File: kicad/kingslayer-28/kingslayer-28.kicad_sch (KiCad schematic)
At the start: 83 parts, among them IC1 STM32F303CCT7, IC3 LM3940IMP-3.3_NOPB, J1 Conn_01x04_Pin, K1 KEYSW, K10 KEYSW, K11 KEYSW, K12 KEYSW, K13 KEYSW, K14 KEYSW, K15 KEYSW, K16 KEYSW, K17 KEYSW, K18 KEYSW, K19 KEYSW, K2 KEYSW, K20 KEYSW, K21 KEYSW, K22 KEYSW, K23 KEYSW, K24 KEYSW, K25 KEYSW, K26 KEYSW, K27 KEYSW, K28 KEYSW, K3 KEYSW, K4 KEYSW, K5 KEYSW, K6 KEYSW, K7 KEYSW, K8 KEYSW, K9 KEYSW, SW1 SS12D07, X1 IC21008.000M30.0EE1B

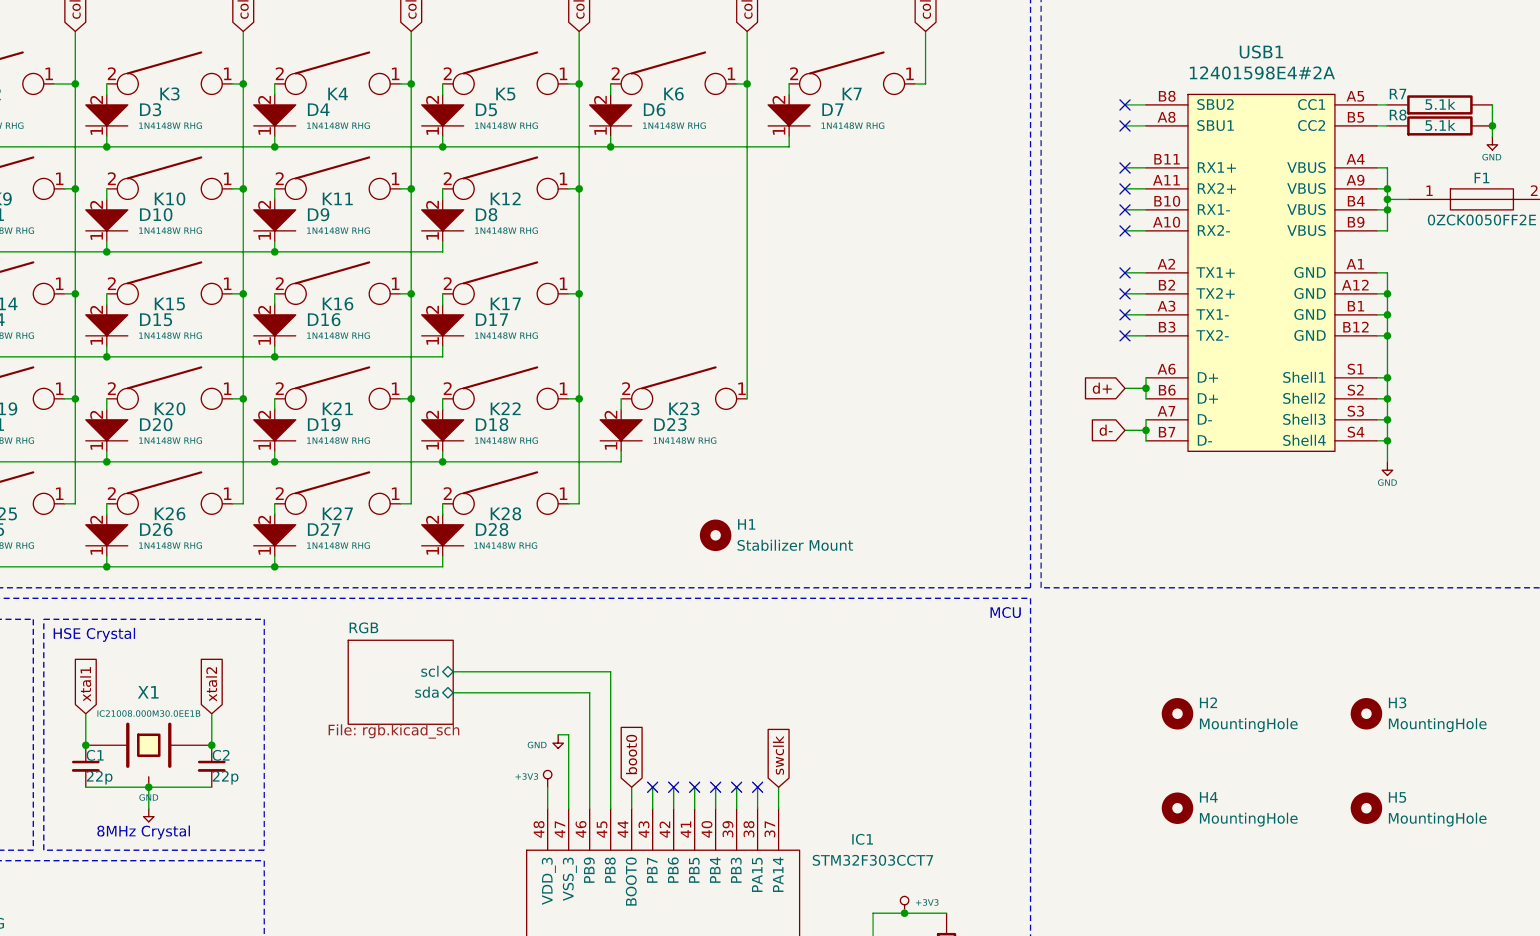
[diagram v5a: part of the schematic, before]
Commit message: finish footprint picking
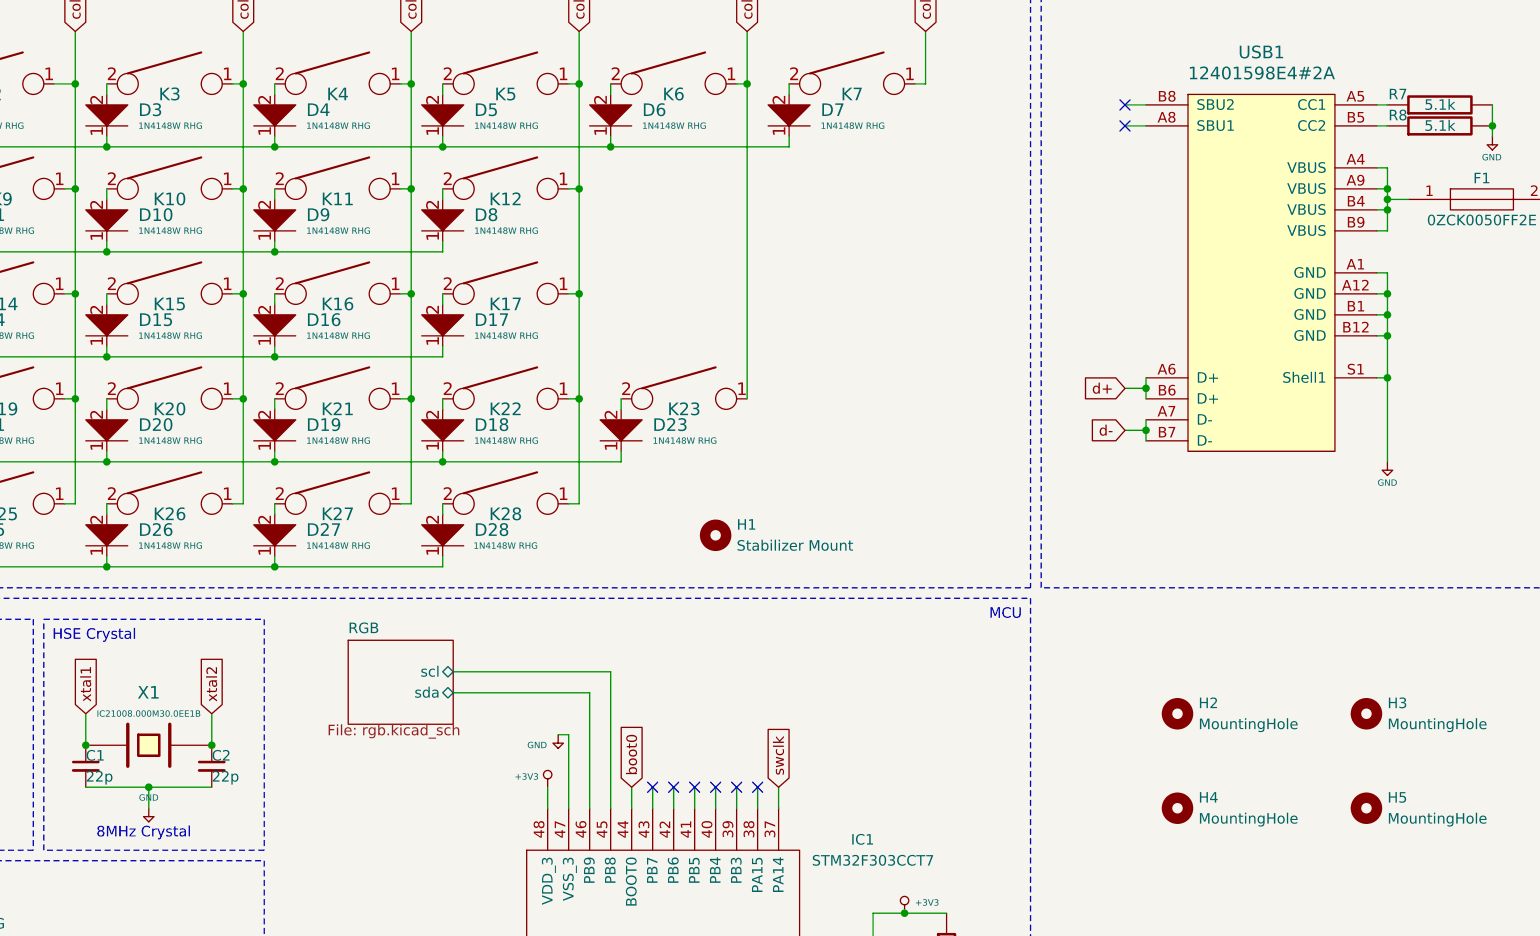
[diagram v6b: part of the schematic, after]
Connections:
- net +5V: no longer USB1.S2 (Shell2), USB1.S3 (Shell3), USB1.S4 (Shell4), X1.3
- no-connect marks 27 -> 19
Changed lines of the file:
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@@
   (junction (at 120.65 64.77) (diameter 0) (color 0 0 0 0)
   )
-  (junction (at 218.44 67.31) (diameter 0) (color 0 0 0 0)
-  )
   (junction (at 76.2 106.68) (diameter 0) (color 0 0 0 0)
   )
@@
   (junction (at 124.46 34.29) (diameter 0) (color 0 0 0 0)
   )
-  (junction (at 218.44 64.77) (diameter 0) (color 0 0 0 0)
-  )
   (junction (at 59.69 52.07) (diameter 0) (color 0 0 0 0)
   )
@@
   (junction (at 140.97 26.67) (diameter 0) (color 0 0 0 0)
   )
-  (junction (at 218.44 69.85) (diameter 0) (color 0 0 0 0)
-  )
   (junction (at 165.1 139.7) (diameter 0) (color 0 0 0 0)
   )
@@
   )
   (no_connect (at 154.94 152.4))
-  (no_connect (at 186.69 54.61))
   (no_connect (at 154.94 144.78))
   (no_connect (at 154.94 154.94))
-  (no_connect (at 186.69 39.37))
   (no_connect (at 137.16 111.76))
   (no_connect (at 129.54 111.76))
   (no_connect (at 154.94 157.48))
-  (no_connect (at 186.69 36.83))
-  (no_connect (at 186.69 52.07))
-  (no_connect (at 186.69 44.45))
-  (no_connect (at 186.69 57.15))
   (no_connect (at 105.41 137.16))
   (no_connect (at 186.69 31.75))
@@
   (no_connect (at 132.08 111.76))
   (no_connect (at 154.94 147.32))
-  (no_connect (at 186.69 49.53))
   (no_connect (at 134.62 111.76))
   (no_connect (at 186.69 29.21))
-  (no_connect (at 186.69 41.91))
   (no_connect (at 139.7 111.76))
   (no_connect (at 154.94 149.86))
@@
     (stroke (width 0) (type default))
   )
-  (wire (pts (xy 186.69 57.15) (xy 189.23 57.15))
-    (stroke (width 0) (type default))
-  )
   (wire (pts (xy 43.18 85.09) (xy 63.5 85.09))
     (stroke (width 0) (type default))
@@
     (stroke (width 0) (type default))
   )
-  (wire (pts (xy 217.17 67.31) (xy 218.44 67.31))
-    (stroke (width 0) (type default))
-  )
   (wire (pts (xy 105.41 97.79) (xy 124.46 97.79))
     (stroke (width 0) (type default))
@@
     (stroke (width 0) (type default))
   )
-  (wire (pts (xy 217.17 69.85) (xy 218.44 69.85))
-    (stroke (width 0) (type default))
-  )
   (wire (pts (xy 139.7 111.76) (xy 139.7 114.3))
     (stroke (width 0) (type default))
@@
     (stroke (width 0) (type default))
   )
-  (wire (pts (xy 186.69 36.83) (xy 189.23 36.83))
-    (stroke (width 0) (type default))
-  )
   (wire (pts (xy 134.62 111.76) (xy 134.62 114.3))
     (stroke (width 0) (type default))
@@
     (stroke (width 0) (type default))
   )
-  (wire (pts (xy 186.69 39.37) (xy 189.23 39.37))
-    (stroke (width 0) (type default))
-  )
   (wire (pts (xy 34.29 133.35) (xy 34.29 135.89))
     (stroke (width 0) (type default))
@@
     (stroke (width 0) (type default))
   )
-  (wire (pts (xy 186.69 49.53) (xy 189.23 49.53))
-    (stroke (width 0) (type default))
-  )
   (wire (pts (xy 21.59 26.67) (xy 21.59 27.94))
     (stroke (width 0) (type default))
@@
     (stroke (width 0) (type default))
   )
-  (wire (pts (xy 218.44 69.85) (xy 218.44 67.31))
-    (stroke (width 0) (type default))
-  )
   (wire (pts (xy 119.38 26.67) (xy 120.65 26.67))
     (stroke (width 0) (type default))
@@
     (stroke (width 0) (type default))
   )
-  (wire (pts (xy 217.17 64.77) (xy 218.44 64.77))
-    (stroke (width 0) (type default))
-  )
   (wire (pts (xy 99.06 26.67) (xy 100.33 26.67))
     (stroke (width 0) (type default))
@@
     (stroke (width 0) (type default))
   )
-  (wire (pts (xy 218.44 64.77) (xy 218.44 62.23))
-    (stroke (width 0) (type default))
-  )
   (wire (pts (xy 134.62 180.34) (xy 134.62 177.8))
     (stroke (width 0) (type default))
@@
     (stroke (width 0) (type default))
   )
-  (wire (pts (xy 186.69 41.91) (xy 189.23 41.91))
-    (stroke (width 0) (type default))
-  )
   (wire (pts (xy 218.44 52.07) (xy 217.17 52.07))
     (stroke (width 0) (type default))
@@
     (stroke (width 0) (type default))
   )
-  (wire (pts (xy 218.44 67.31) (xy 218.44 64.77))
-    (stroke (width 0) (type default))
-  )
   (wire (pts (xy 120.65 64.77) (xy 119.38 64.77))
     (stroke (width 0) (type default))
@@
     (stroke (width 0) (type default))
   )
-  (wire (pts (xy 186.69 52.07) (xy 189.23 52.07))
-    (stroke (width 0) (type default))
-  )
   (wire (pts (xy 106.68 160.02) (xy 109.22 160.02))
     (stroke (width 0) (type default))
@@
     (stroke (width 0) (type default))
   )
-  (wire (pts (xy 186.69 54.61) (xy 189.23 54.61))
-    (stroke (width 0) (type default))
-  )
   (wire (pts (xy 83.82 52.07) (xy 83.82 53.34))
     (stroke (width 0) (type default))
@@
     (stroke (width 0) (type default))
   )
-  (wire (pts (xy 218.44 72.39) (xy 218.44 69.85))
+  (wire (pts (xy 218.44 62.23) (xy 218.44 72.39))
     (stroke (width 0) (type default))
   )
@@
     (stroke (width 0) (type default))
   )
-  (wire (pts (xy 186.69 44.45) (xy 189.23 44.45))
-    (stroke (width 0) (type default))
-  )
   (wire (pts (xy 132.08 111.76) (xy 132.08 114.3))
     (stroke (width 0) (type default))
@@
     (pin "1")
     (pin "2")
-    (pin "3")
     (instances
       (project "kingslayer-28"
@@
     )
     (pin "A1")
-    (pin "A10")
-    (pin "A11")
     (pin "A12")
-    (pin "A2")
-    (pin "A3")
     (pin "A4")
     (pin "A5")
@@
     (pin "A9")
     (pin "B1")
-    (pin "B10")
-    (pin "B11")
     (pin "B12")
-    (pin "B2")
-    (pin "B3")
     (pin "B4")
     (pin "B5")
@@
     (pin "B9")
     (pin "S1")
-    (pin "S2")
-    (pin "S3")
-    (pin "S4")
     (instances
       (project "kingslayer-28"

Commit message: initial placement
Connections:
- net +5V: no longer C1.2, C10.1, C11.2, C12.1, C12.2, C2.2, C3.1, C3.2, C4.1, C4.2, C5.1, C5.2, C6.1, C6.2, C7.1, C7.2, IC1.1 (VBAT), IC1.23 (VSS_1), IC1.24 (VDD_1), IC1.35 (VSS_2), IC1.36 (VDD_2), IC1.47 (VSS_3), IC1.48 (VDD_3), IC1.8 (VSSA/VREF-), IC1.9 (VDDA), IC3.2 (GND_1), IC3.3 (OUT), IC3.4 (GND_2), J1.1 (Pin_1), J1.4 (Pin_4), R7.2, R8.2, R9.1, S1.1, S1.3, SW1.1 (A), SW1.3 (C), USB1.A1 (GND), USB1.A12 (GND), USB1.B1 (GND), USB1.B12 (GND), USB1.S1 (Shell1)
- new net +3V3: C12.1, C3.1, C4.1, C5.1, C6.1, C7.1, IC1.1 (VBAT), IC1.24 (VDD_1), IC1.36 (VDD_2), IC1.48 (VDD_3), IC1.9 (VDDA), IC3.3 (OUT), J1.4 (Pin_4), R9.1, SW1.3 (C)
- new net GND: C1.2, C10.1, C11.2, C12.2, C2.2, C3.2, C4.2, C5.2, C6.2, C7.2, IC1.23 (VSS_1), IC1.35 (VSS_2), IC1.47 (VSS_3), IC1.8 (VSSA/VREF-), IC3.2 (GND_1), IC3.4 (GND_2), J1.1 (Pin_1), R7.2, R8.2, S1.1, S1.3, SW1.1 (A), USB1.A1 (GND), USB1.A12 (GND), USB1.B1 (GND), USB1.B12 (GND), USB1.S1 (Shell1)

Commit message: 3d model
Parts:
- USB1: footprint Type-C:USB_C_GCT_USB4085 -> custom:USB_C_GCT_USB4085
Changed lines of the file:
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@@
       (effects (font (size 1.524 1.524)))
     )
-    (property "Footprint" "Type-C:USB_C_GCT_USB4085" (at 185.42 49.53 0)
+    (property "Footprint" "custom:USB_C_GCT_USB4085" (at 185.42 49.53 0)
       (effects (font (size 1.524 1.524)) hide)
     )
